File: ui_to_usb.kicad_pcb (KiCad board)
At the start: 2 copper layers, 39.2 x 29 mm, 41 parts, among them J1 PM254-2-06-S-8.5, J2 TYPE-C-31-M-12, U1 FT232H, U2 93LC56C, U3 USBLC6-2SC6, Y2 12M

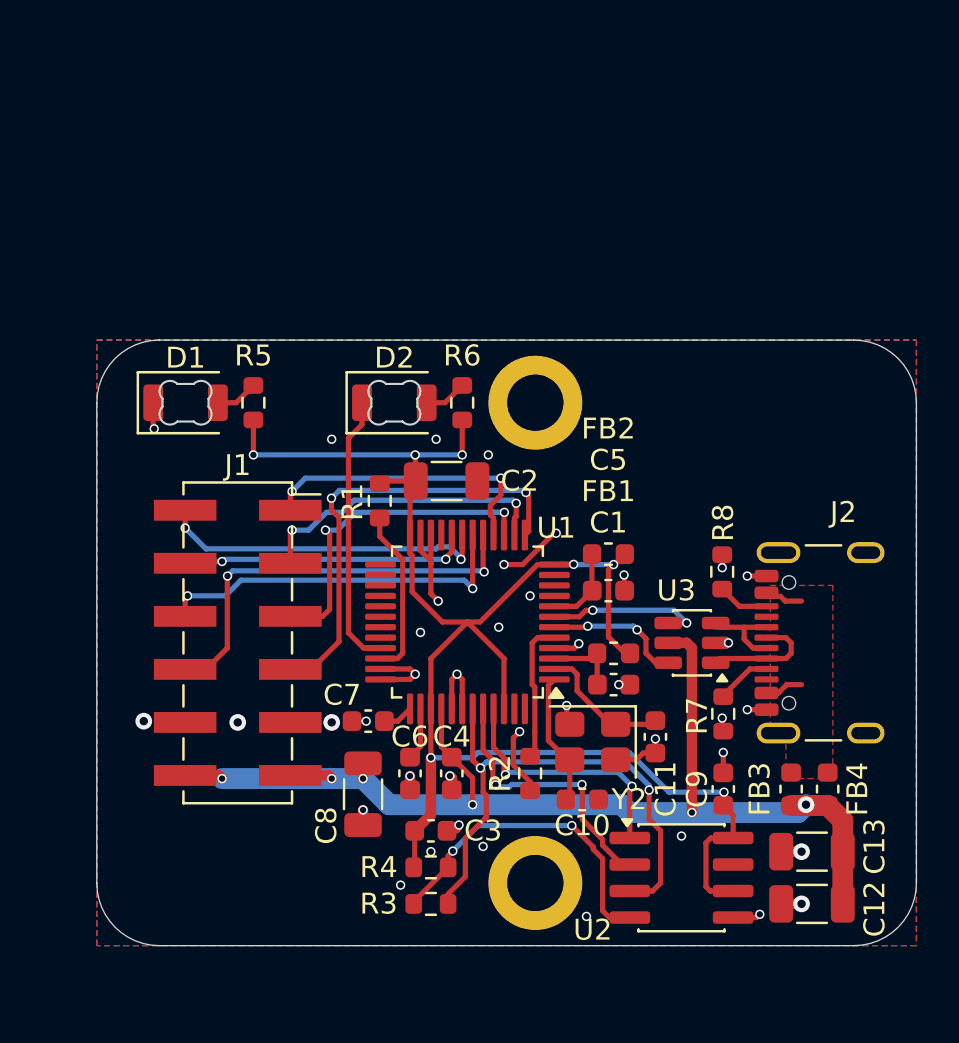
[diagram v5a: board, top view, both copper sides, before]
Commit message: switch to CH32V203
as the V305 I've selected before doesn't have a BOOT0 pin
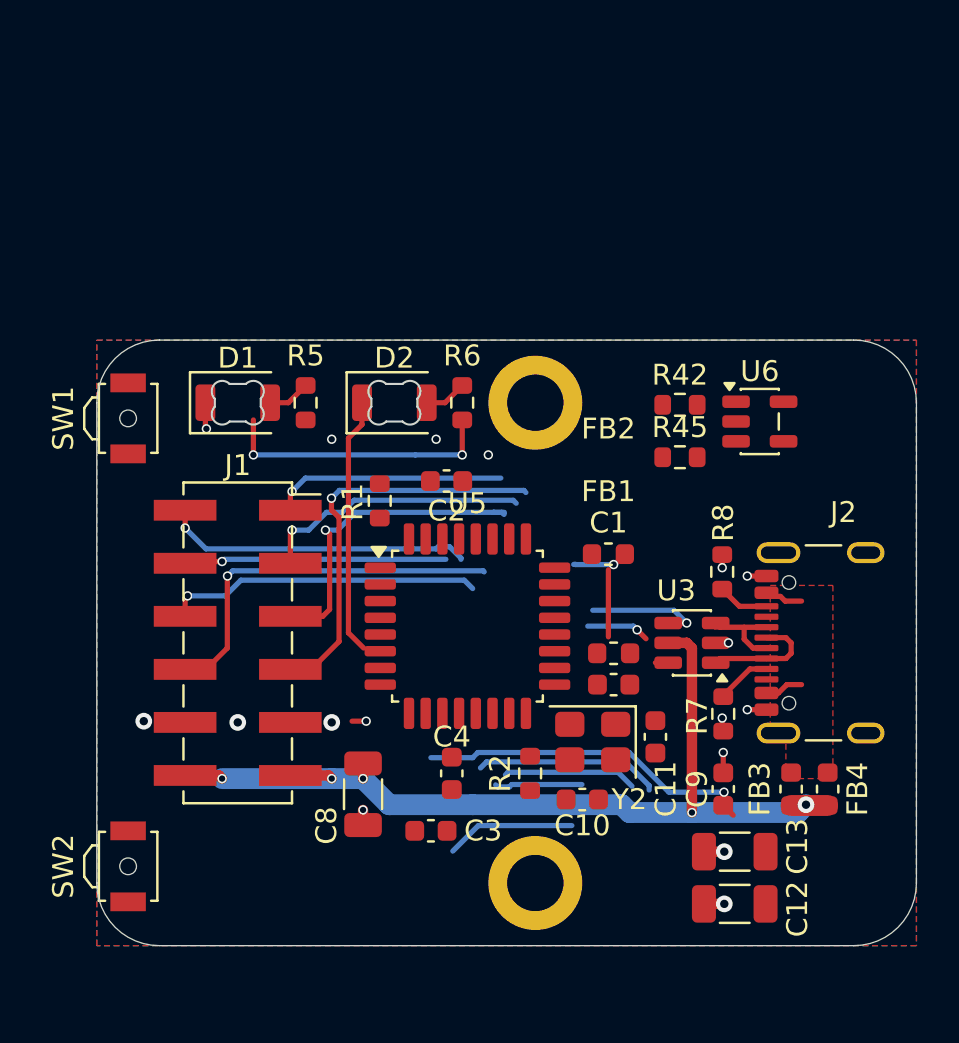
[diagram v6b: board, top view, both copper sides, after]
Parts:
- removed C5, C6, C7: 1u, Capacitor_SMD:C_0603_1608Metric
- removed R3: 2k, Resistor_SMD:R_0603_1608Metric
- removed R4: 10k, Resistor_SMD:R_0603_1608Metric
- removed U1: FT232H, Package_QFP:LQFP-48_7x7mm_P0.5mm
- removed U2: 93LC56C, Package_SO:SOIC-8_3.9x4.9mm_P1.27mm
- added R42: 37k4, Resistor_SMD:R_0603_1608Metric, F.Cu at (102.2, 68.6)
- added R45: 22k, Resistor_SMD:R_0603_1608Metric, F.Cu at (102.2, 71.1)
- added SW1: RST, Button_Switch_SMD:SW_SPST_B3U-3000P-B, F.Cu at (75.8, 69.3)
- added SW2: BOOT, Button_Switch_SMD:SW_SPST_B3U-3000P-B, F.Cu at (75.8, 90.7)
- added U5: CH32V203KxT6, Package_QFP:LQFP-32_7x7mm_P0.8mm, F.Cu at (92.0, 79.2)
- added U6: SPX3819M5-L, Package_TO_SOT_SMD:SOT-23-5, F.Cu at (106.0, 69.4)
- C1: value 1u -> 100n
- C2: value 10u -> 1u; footprint Capacitor_SMD:C_1206_3216Metric -> Capacitor_SMD:C_0603_1608Metric
- R2: value 12k -> 10k
- R5, R6: value 1k5 -> 10k
- Y2: value 12M -> 8M
- moved C12 3.70 mm to (104.8, 92.5)
- moved C13 3.70 mm to (104.8, 90.0)
- moved D1 2.50 mm to (81.0, 68.5)
- moved R5 2.50 mm to (84.3, 68.5)
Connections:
- C1 pad 1: Net-(U1-VPHY) -> GND
- C1 pad 2: GND -> /RST_N
- C2 pad 1: GND -> +3V3
- C2 pad 2: +3.3V -> GND
- C3 pad 2: +3.3V -> Net-(U5-VDDA)
- C9 pad 2: +3.3V -> VDD
- FB1 pad 1: Net-(U1-VPHY) -> +3.3V
- FB1 pad 2: +3.3V -> Net-(U5-VDDA)
- FB2 pad 1: Net-(U1-VPLL) -> +3.3V
- FB2 pad 2: +3.3V -> VDD
- R1 pad 1: +3.3V -> /RST_N
- R1 pad 2: Net-(U1-~{RESET}) -> +3.3V
- R2 pad 2: Net-(U1-REF) -> /BOOT0
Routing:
- net +3.3V: track 79.2 -> 13.3 mm, vias 7 -> 2
- net GND: track 37.3 -> 9.30 mm, vias 40 -> 17
- net (no net): track 0.00 -> 25.7 mm
- net Net-(U1-EEDATA): track 25.6 -> 0.00 mm, vias 2 -> 0
- net VDD: track 0.00 -> 18.9 mm, vias 0 -> 2
- net Net-(U2-DO): track 15.6 -> 0.00 mm, vias 2 -> 0
- net /EECLK: track 13.1 -> 0.00 mm, vias 2 -> 0
- net /EECS: track 12.3 -> 0.00 mm, vias 2 -> 0
- net +5V: track 56.3 -> 46.0 mm, vias 6 -> 5
- net Net-(U1-~{RESET}): track 8.10 -> 0.00 mm
- net Net-(U1-REF): track 6.73 -> 0.00 mm
- net Net-(U5-OSC_OUT/PD1): track 6.48 -> 0.00 mm
- net Net-(U5-OSC_IN/PD0): track 6.43 -> 0.00 mm
- net Net-(U1-VPLL): track 3.88 -> 0.00 mm
- net Net-(U1-VPHY): track 3.66 -> 0.00 mm
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
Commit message: add extension port
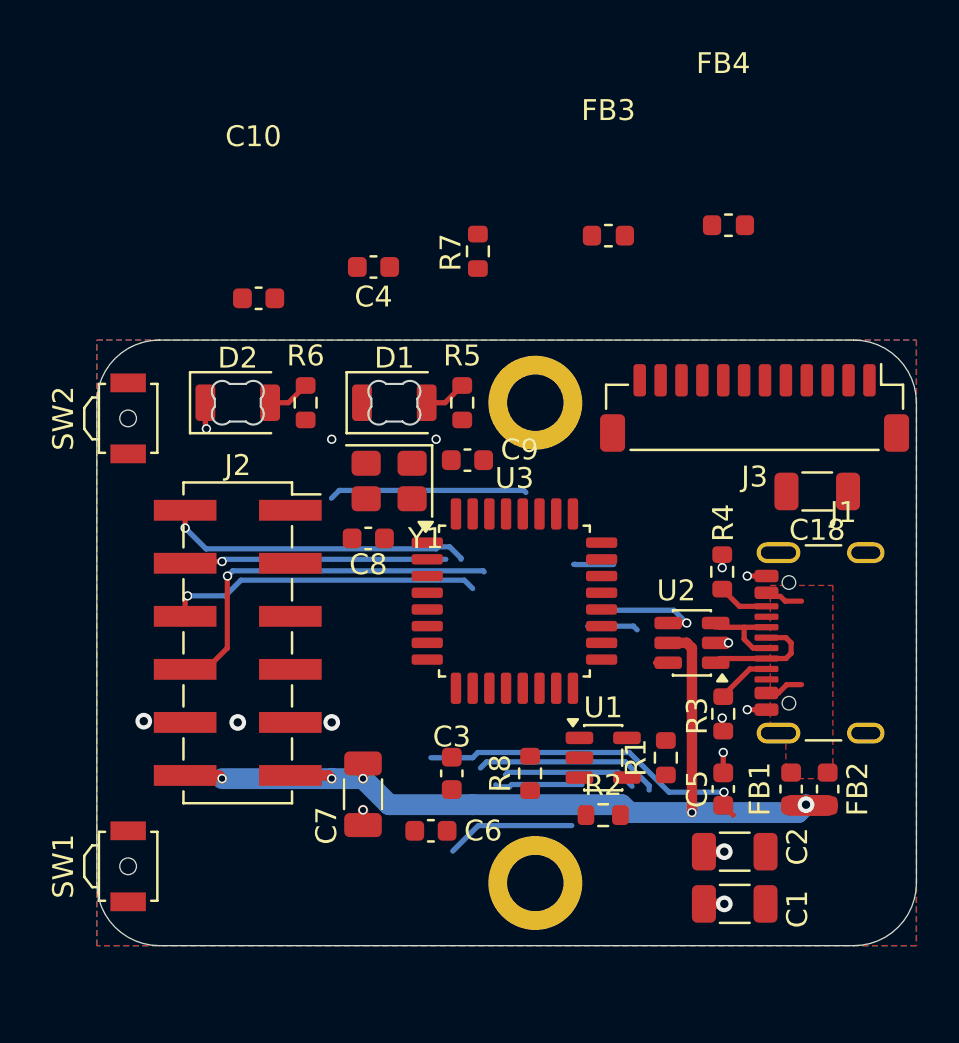
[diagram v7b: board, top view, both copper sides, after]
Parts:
- added C18: 10u, Capacitor_SMD:C_1206_3216Metric, F.Cu at (108.8, 72.8)
- added J3: BM12B-SRSS-TB, Connector_JST:JST_SH_BM12B-SRSS-TB_1x12-1MP_P1.00mm_Vertical, F.Cu at (105.8, 68.8)
- SW1: renamed from SW2; value BOOT -> BOOT0
- U3: renamed from U5; value CH32V203KxT6 -> CH32V203K8T6
- moved C10 25.1 mm to (82.0, 63.5)
- moved FB4 21.2 mm to (104.5, 60.0)
- moved U1 17.8 mm to (98.5, 85.5)
- moved R2 17.5 mm to (98.5, 88.3)
- moved R1 16.9 mm to (101.5, 85.5), turned to 90 degrees
- moved C8 16.2 mm to (87.3, 75.0)
- moved C9 16.0 mm to (92.0, 71.3), turned to 180 degrees
- moved Y1 15.9 mm to (88.3, 72.3)
- moved FB3 15.2 mm to (98.8, 60.5)
- moved R7 12.8 mm to (92.5, 61.3)
- moved C4 10.8 mm to (87.5, 62.0)
- moved U3 2.55 mm to (94.3, 78.0)
- renumbered C12 to C1, C1 to C10, C13 to C2, C4 to C3, C2 to C4, C9 to C5, C3 to C6, C8 to C7, C10 to C8, C11 to C9, D2 to D1, D1 to D2, FB3 to FB1, FB4 to FB2, FB2 to FB3, FB1 to FB4, J2 to J1, J1 to J2, R42 to R1, R45 to R2, R7 to R3, R8 to R4, R6 to R5, R5 to R6, R1 to R7, R2 to R8, SW1 to SW2, U6 to U1, U3 to U2, Y2 to Y1
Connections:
- U3 pad 14: unconnected-(U5-PB0-Pad14) -> /PB0
- U3 pad 15: unconnected-(U5-PB1-Pad15) -> /PB1
- U3 pad 18: unconnected-(U5-PA8-Pad18) -> /PA8
- U3 pad 23: unconnected-(U5-PA13/SWDIO-Pad23) -> /PA13
- U3 pad 24: unconnected-(U5-PA14/SWCLK-Pad24) -> /PA14
- U3 pad 26: unconnected-(U5-PB3-Pad26) -> /PB3
- U3 pad 27: unconnected-(U5-PB4-Pad27) -> /PB4
- U3 pad 28: unconnected-(U5-PB5-Pad28) -> /PB5
- U3 pad 29: unconnected-(U5-PB6-Pad29) -> /PB6
- U3 pad 30: unconnected-(U5-PB7-Pad30) -> /PB7
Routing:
- net /SDI: track 15.4 -> 0.00 mm, vias 1 -> 0
- net +3.3V: track 13.3 -> 0.00 mm, vias 2 -> 0
- net /SDO: track 13.0 -> 0.00 mm, vias 1 -> 0
- net Net-(D1-K): track 12.3 -> 0.00 mm
- net /CS_OLED_N: track 11.2 -> 0.00 mm, vias 1 -> 0
- net /SCK: track 19.4 -> 9.51 mm, vias 1 -> 0
- net Net-(U3-VDDA): track 3.21 -> 0.00 mm
- net VDD: track 18.9 -> 18.2 mm, vias 2 -> 1
- net GND: track 9.30 -> 8.62 mm, vias 17 -> 15
- net /D_N: track 3.65 -> 3.05 mm, vias 1 -> 0
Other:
- board text added: "Rev: 1 02/2026"
- board text removed: "Rev: - 12/2025"

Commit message: explore placement
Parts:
- added C11: 1u, Capacitor_SMD:C_0603_1608Metric, F.Cu at (87.5, 77.3)
- moved C4 30.6 mm to (102.0, 89.0), turned to -90 degrees
- moved R7 29.9 mm to (84.3, 90.0), turned to 180 degrees
- moved C10 29.2 mm to (85.0, 92.5), turned to 90 degrees
- moved FB4 27.8 mm to (87.5, 82.0)
- moved SW2 27.0 mm to (88.5, 93.0), turned to 180 degrees
- moved FB3 25.5 mm to (102.0, 85.8), turned to 90 degrees
- moved R8 14.5 mm to (81.0, 90.0), turned to 0 degrees
- moved C3 12.2 mm to (102.0, 92.0)
- moved C6 9.17 mm to (87.5, 80.3), turned to 0 degrees
- moved R2 8.84 mm to (107.3, 87.0), turned to -90 degrees
- moved U1 7.70 mm to (104.8, 90.0), turned to 90 degrees
- moved SW1 5.73 mm to (81.0, 93.0), turned to 180 degrees
- moved C1 4.95 mm to (109.8, 92.5), turned to 180 degrees
- moved C2 4.95 mm to (109.8, 90.0), turned to 180 degrees
- moved C5 4.19 mm to (100.3, 85.8), turned to 90 degrees
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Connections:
- FB3 pad 1: +3.3V -> +3V3
- FB4 pad 1: +3.3V -> +3V3
- J3 pad 10: /PA8 -> /PA13
- J3 pad 11: /PA13 -> /PA14
- J3 pad 12: /PA14 -> /PA15
- R7 pad 2: +3.3V -> +3V3
- SW1 pad 2: +3.3V -> +3V3
- U3 pad 18: /PA8 -> Net-(D1-K)
- U3 pad 25: Net-(D1-K) -> /PA15
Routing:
- net (no net): track 25.7 -> 0.00 mm
- net /D_C: track 18.3 -> 0.00 mm, vias 1 -> 0
- net +5V: track 46.0 -> 29.8 mm, vias 5 -> 2
- net /CS_IO_N: track 15.2 -> 0.00 mm, vias 1 -> 0
- net /INT_IO: track 14.8 -> 0.00 mm, vias 1 -> 0
- net VDD: track 18.2 -> 4.48 mm, vias 1 -> 0
- net /RES_N: track 12.6 -> 0.00 mm, vias 1 -> 0
- net Net-(U3-OSC_OUT/PD1): track 0.00 -> 10.5 mm, vias 0 -> 2
- net /SCK: track 9.51 -> 0.00 mm
- net Net-(U3-OSC_IN/PD0): track 0.00 -> 7.37 mm, vias 0 -> 2
- net /D_P: track 5.64 -> 0.00 mm, vias 1 -> 0
- net +3V3: track 0.00 -> 5.41 mm, vias 0 -> 1
- net Net-(U1-ADJ): track 0.00 -> 3.50 mm
- net /D_N: track 3.05 -> 0.00 mm
- net GND: track 8.62 -> 6.35 mm, vias 15 -> 10
- added copper zone on F.Cu, net +5V
